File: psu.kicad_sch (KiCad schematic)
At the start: 42 parts, among them U1 LT8653S, U2 LT8636

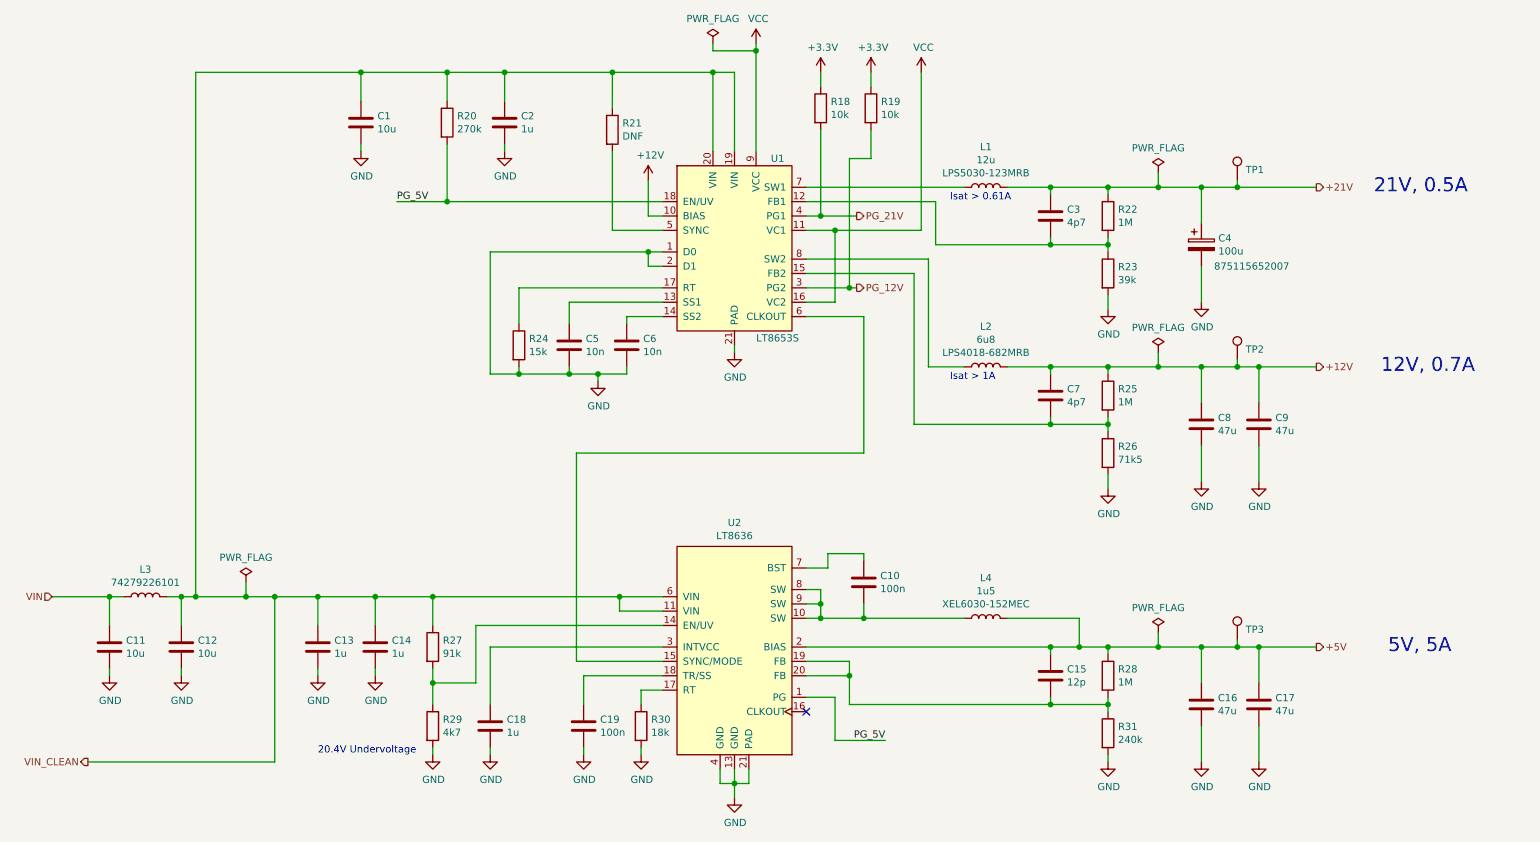
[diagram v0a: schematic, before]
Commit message: Started new connector layout
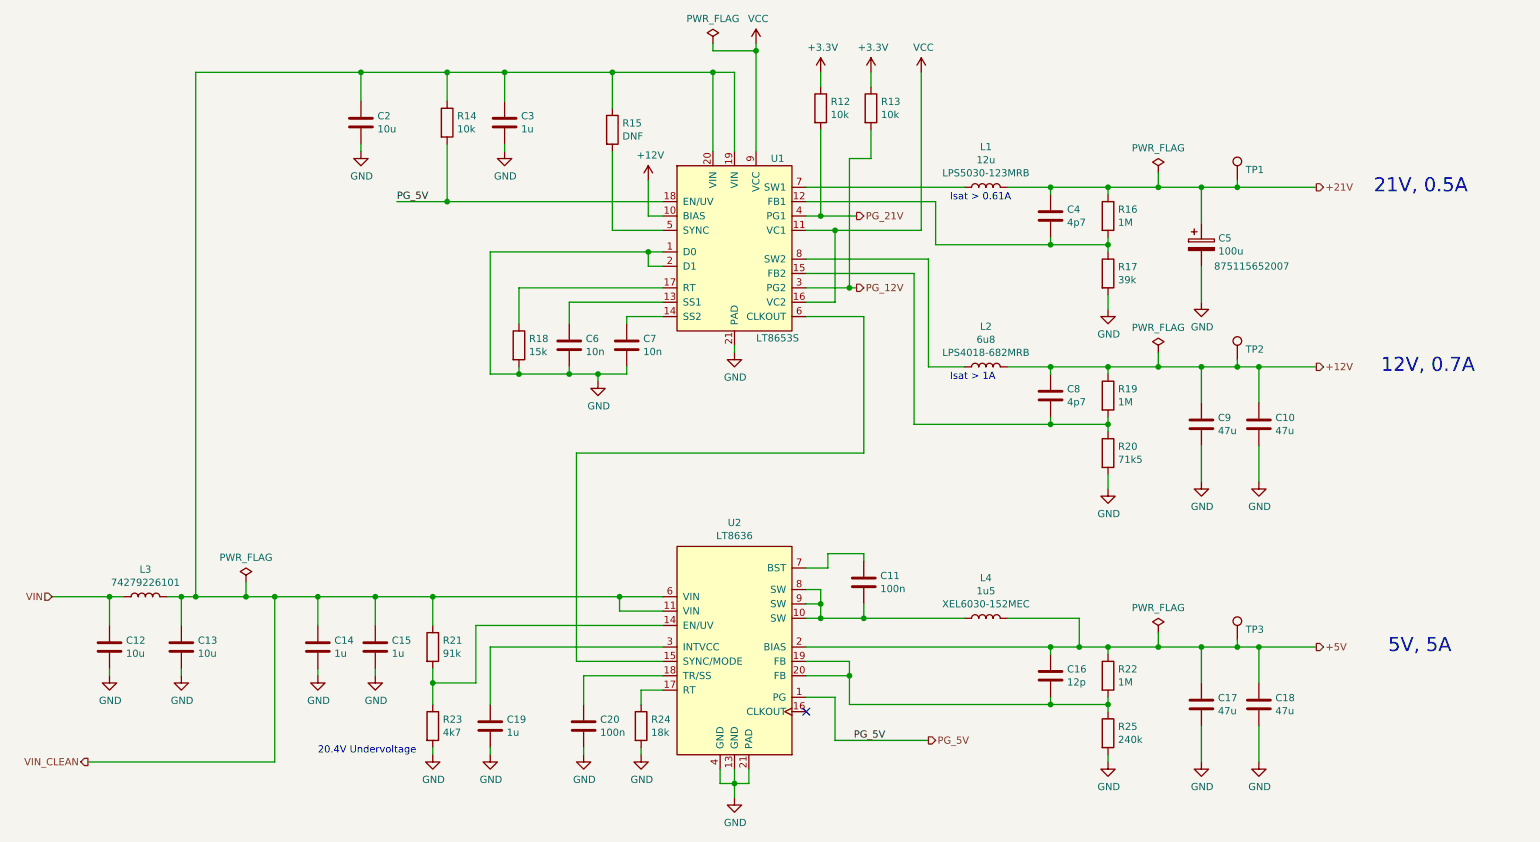
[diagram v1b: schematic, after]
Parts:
- R14: renamed from R20; value 270k -> 10k
- renumbered C9 to C10, C10 to C11, C11 to C12, C12 to C13, C13 to C14, C14 to C15, C15 to C16, C16 to C17, C17 to C18, C18 to C19, C1 to C2, C19 to C20, C2 to C3, C3 to C4, C4 to C5, C5 to C6, C6 to C7, C7 to C8, C8 to C9, R18 to R12, R19 to R13, R21 to R15, R22 to R16, R23 to R17, R24 to R18, R25 to R19, R26 to R20, R27 to R21, R28 to R22, R29 to R23, R30 to R24, R31 to R25

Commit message: Mostly complete, just missing a few tracks and review
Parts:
- C11, C14, C15, C16, C19, C20, C3: footprint Capacitor_SMD:C_0402_1005Metric -> Capacitor_SMD:C_0603_1608Metric
- C4: renamed from C8; footprint Capacitor_SMD:C_0402_1005Metric -> Capacitor_SMD:C_0603_1608Metric
- C7: renamed from C6; footprint Capacitor_SMD:C_0402_1005Metric -> Capacitor_SMD:C_0603_1608Metric
- C8: renamed from C7; footprint Capacitor_SMD:C_0402_1005Metric -> Capacitor_SMD:C_0603_1608Metric
- C9: renamed from C4; footprint Capacitor_SMD:C_0402_1005Metric -> Capacitor_SMD:C_0603_1608Metric
- R17: renamed from R12; footprint Resistor_SMD:R_0402_1005Metric -> Resistor_SMD:R_0603_1608Metric
- R18: renamed from R13; footprint Resistor_SMD:R_0402_1005Metric -> Resistor_SMD:R_0603_1608Metric
- R19: renamed from R14; footprint Resistor_SMD:R_0402_1005Metric -> Resistor_SMD:R_0603_1608Metric
- R20: renamed from R15; footprint Resistor_SMD:R_0402_1005Metric -> Resistor_SMD:R_0603_1608Metric
- R21: renamed from R19; footprint Resistor_SMD:R_0402_1005Metric -> Resistor_SMD:R_0603_1608Metric
- R22: renamed from R20; footprint Resistor_SMD:R_0402_1005Metric -> Resistor_SMD:R_0603_1608Metric
- R23: renamed from R18; footprint Resistor_SMD:R_0402_1005Metric -> Resistor_SMD:R_0603_1608Metric
- R24: renamed from R16; footprint Resistor_SMD:R_0402_1005Metric -> Resistor_SMD:R_0603_1608Metric
- R25: renamed from R17; footprint Resistor_SMD:R_0402_1005Metric -> Resistor_SMD:R_0603_1608Metric
- R26: renamed from R21; footprint Resistor_SMD:R_0402_1005Metric -> Resistor_SMD:R_0603_1608Metric
- R27: renamed from R22; footprint Resistor_SMD:R_0402_1005Metric -> Resistor_SMD:R_0603_1608Metric
- R28: renamed from R23; footprint Resistor_SMD:R_0402_1005Metric -> Resistor_SMD:R_0603_1608Metric
- R29: renamed from R24; footprint Resistor_SMD:R_0402_1005Metric -> Resistor_SMD:R_0603_1608Metric
- R30: renamed from R25; footprint Resistor_SMD:R_0402_1005Metric -> Resistor_SMD:R_0603_1608Metric
- renumbered C5 to C10, C9 to C5, C10 to C6, L2 to L1, L1 to L2, TP2 to TP1, TP1 to TP2
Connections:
- net GND: now also R30.1; no longer R30.2
- net PG_12V: now also R17.2, U1.4 (PG1); no longer R18.2, U1.3 (PG2)
- net PG_21V: now also R18.2, U1.3 (PG2); no longer R17.2, U1.4 (PG1)
- net at C16.2, R27.2, U2.19 (FB)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: now also R30.2; no longer R30.1
- net at C9.2, R24.2, R25.1: now also U1.15 (FB2); no longer U1.12 (FB1)
- net at C4.2, R21.2, R22.1: now also U1.12 (FB1); no longer U1.15 (FB2)
- net at U1.7 (SW1): now also L1.1; no longer L2.1
- net at U1.8 (SW2): now also L2.1; no longer L1.1
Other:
- moved on the sheet: C10, C4, C5, C6, C9, L1, L2, R21, R22, R24, R25, TP1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

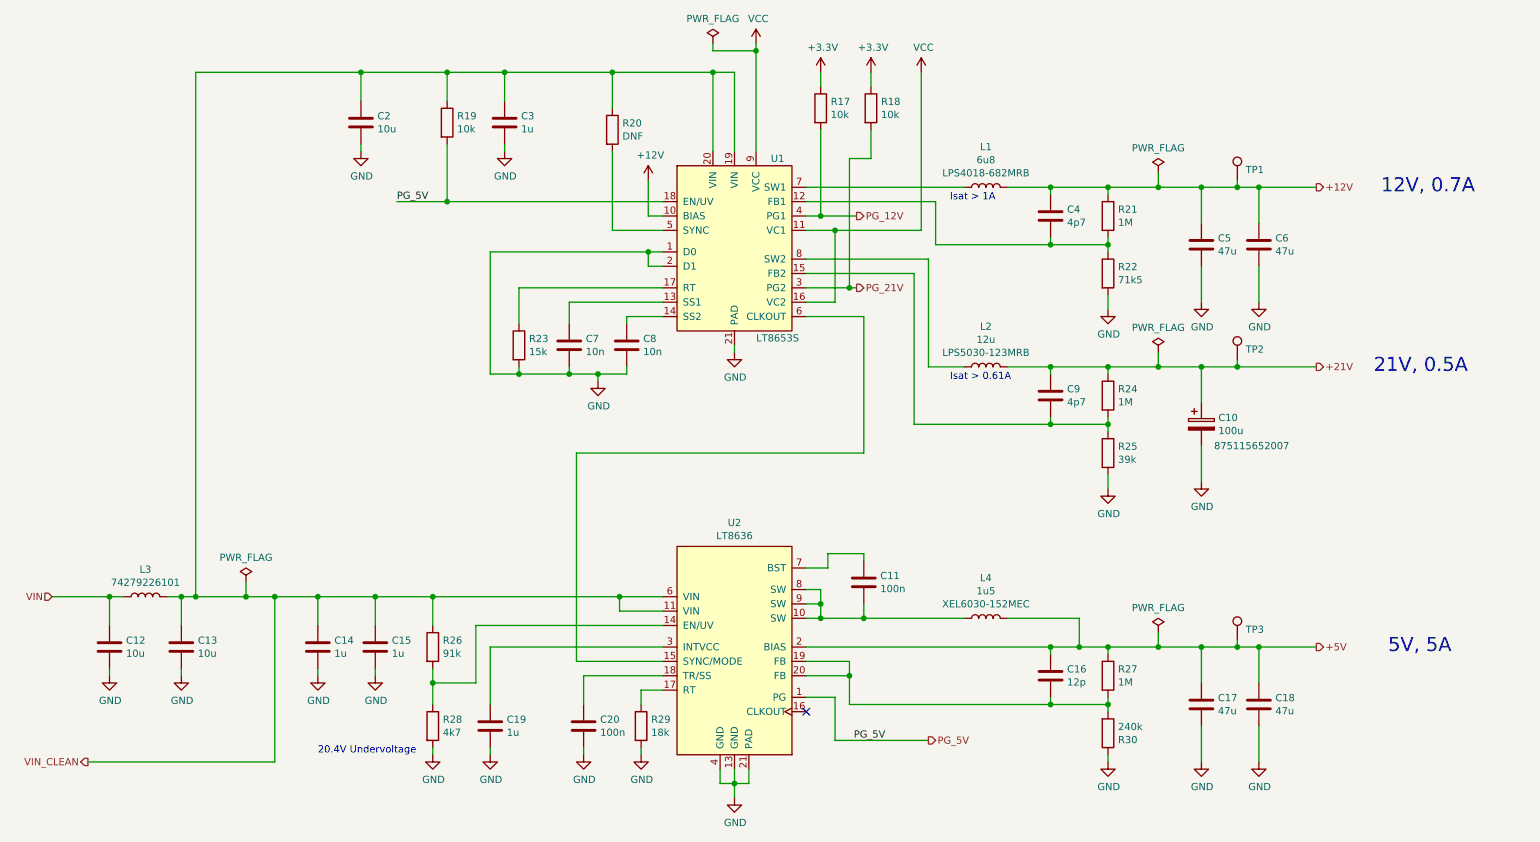
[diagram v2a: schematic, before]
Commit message: Finished tidying up silkscreen
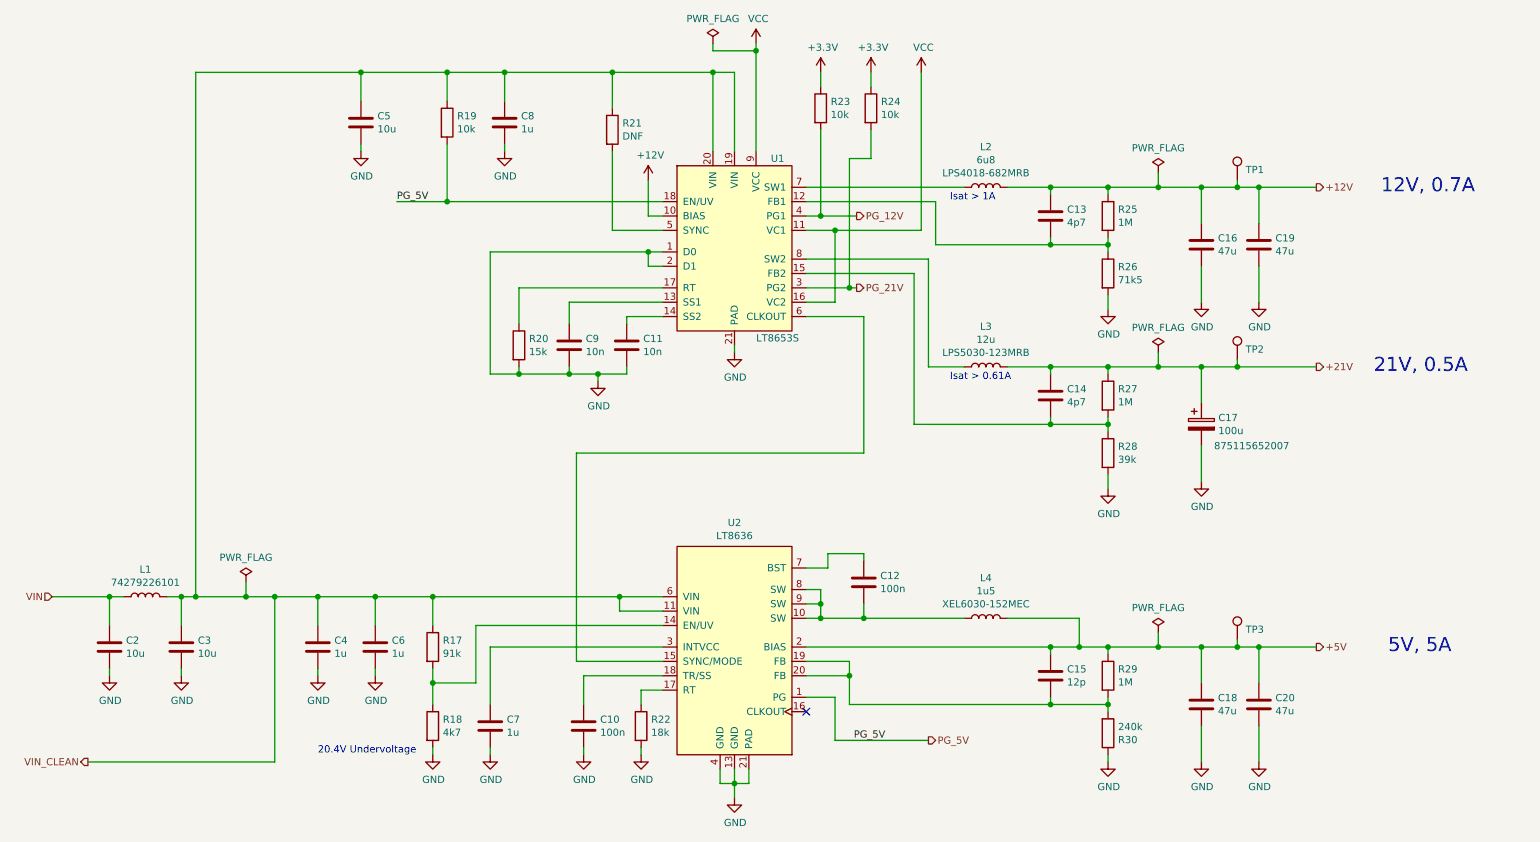
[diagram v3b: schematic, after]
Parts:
- renumbered C20 to C10, C8 to C11, C11 to C12, C4 to C13, C9 to C14, C16 to C15, C5 to C16, C10 to C17, C17 to C18, C6 to C19, C12 to C2, C18 to C20, C13 to C3, C14 to C4, C2 to C5, C15 to C6, C19 to C7, C3 to C8, C7 to C9, L3 to L1, L1 to L2, L2 to L3, R26 to R17, R28 to R18, R23 to R20, R20 to R21, R29 to R22, R17 to R23, R18 to R24, R21 to R25, R22 to R26, R24 to R27, R25 to R28, R27 to R29

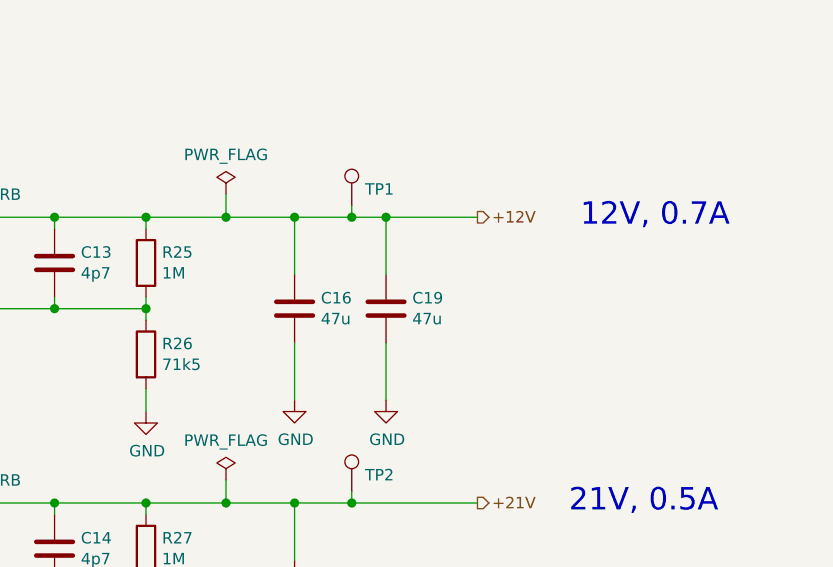
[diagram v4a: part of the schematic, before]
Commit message: Tweaked component values to working. Added rear panel PCB
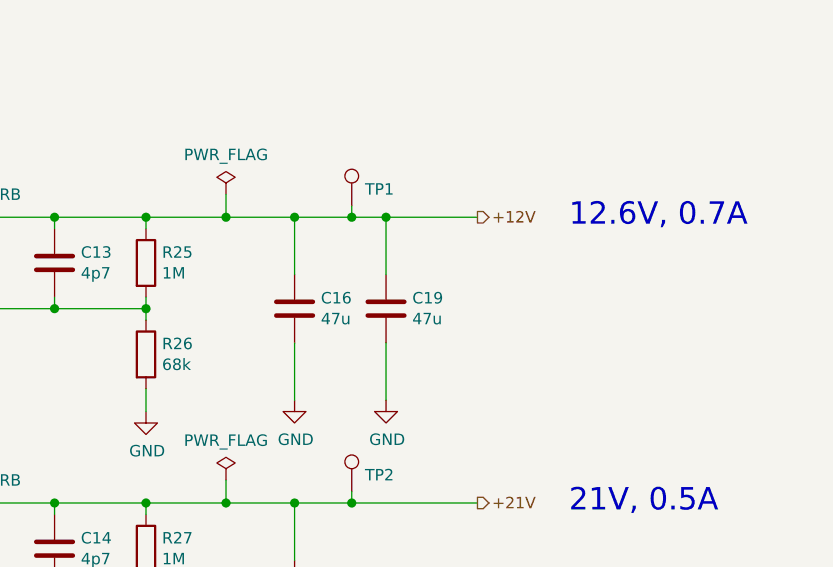
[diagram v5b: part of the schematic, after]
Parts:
- R26: value 71k5 -> 68k
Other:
- note added: "12.6V, 0.7A"
- note removed: "12V, 0.7A"
